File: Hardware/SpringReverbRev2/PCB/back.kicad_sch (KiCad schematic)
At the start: 54 parts, among them IC102 TL074, IC103 TL074, J901 AudioJack2_SwitchT, J902 AudioJack2, J903 AudioJack2, J904 AudioJack2, J905 AudioJack2_SwitchT, J906 AudioJack2, U7 NE5532, U901 L78L05_TO92, X101 RCA, X102 RCA

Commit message: misc corrections
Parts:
- C1, C2: value 10uf -> 10uF; footprint ao_tht:CP_Radial_D6.3mm_P2.50mm -> ao_tht:C_Disc_D3.0mm_W1.6mm_P2.50mm; symbol ao_symbols:CP -> ao_symbols:C
- C101, C109: footprint ao_tht:CP_Radial_D6.3mm_P2.50mm -> ao_tht:C_Disc_D3.0mm_W1.6mm_P2.50mm; symbol ao_symbols:CP -> ao_symbols:C
- C104, C105, C106, C107, C901, C902: value 100n -> 100nF
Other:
- note added: "R109 and R107 set recovery level R107 should be smaller than output coil impedance [sic] 2250/2575Ω: R107 = 22Ω R109 = 22K Increase R109 for stronger output, reduce R109 if circuit distorts even when spring drive is set low."
- note added: "Values for VR1: 800Ω tank: VR1 = 2k 150Ω tank: VR1 = 470Ω Or use 10k trimmer For larger input impedances, try a larger trimmer."
- note removed: "R109 and R107 set recovery level R107 should be smaller than output coil impedance 2250/2575Ω: R107 = 22Ω R109 = 22K Increase R109 for stronger output, reduce R109 if circuit distorts even when spring drive is set low."
- note removed: "Values for R103: 800Ω tank: R103 = 2k 150Ω tank: R103 = 470Ω Or use 10k trimmer For larger input impedances, try a larger trimmer."
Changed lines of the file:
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@@
     (effects (font (size 1.778 1.5113)) (justify left bottom))
   )
-  (text "R109 and R107 set recovery level\nR107 should be smaller than\noutput coil impedance\n2250/2575Ω: R107 = 22Ω R109 = 22K\nIncrease R109 for stronger output,\nreduce R109 if circuit distorts even when\nspring drive is set low."
+  (text "R109 and R107 set recovery level\nR107 should be smaller than\noutput coil impedance [sic]\n2250/2575Ω: R107 = 22Ω R109 = 22K\nIncrease R109 for stronger output,\nreduce R109 if circuit distorts even when\nspring drive is set low."
     (at 89.535 173.355 0)
     (effects (font (size 1.778 1.5113)) (justify left bottom))
@@
     (effects (font (size 1.778 1.5113)) (justify left bottom))
   )
-  (text "Values for R103:\n800Ω tank: R103 = 2k\n150Ω tank: R103 = 470Ω\nOr use 10k trimmer\nFor larger input impedances,\ntry a larger trimmer."
+  (text "Values for VR1:\n800Ω tank: VR1 = 2k\n150Ω tank: VR1 = 470Ω\nOr use 10k trimmer\nFor larger input impedances,\ntry a larger trimmer."
     (at 48.26 153.67 0)
     (effects (font (size 1.778 1.5113)) (justify left top))
@@
       (effects (font (size 1.27 1.27)) (justify left))
     )
-    (property "Value" "100n" (id 1) (at 215.646 102.0322 0)
+    (property "Value" "100nF" (id 1) (at 215.646 102.0322 0)
       (effects (font (size 1.27 1.27)) (justify left))
     )
@@
     )
     (property "Vendor" "Tayda" (id 4) (at 212.725 100.33 0)
+      (effects (font (size 1.27 1.27)) hide)
+    )
+    (property "Description" "Ceramic capacitor" (id 5) (at 212.725 100.33 0)
       (effects (font (size 1.27 1.27)) hide)
     )
@@
       (effects (font (size 1.27 1.27)) hide)
     )
+    (property "Description" "Polyester film capacitor" (id 5) (at 222.25 41.91 0)
+      (effects (font (size 1.27 1.27)) hide)
+    )
     (pin "1")
     (pin "2")
@@
     (pin "2")
   )
-  (symbol (lib_id "ao_symbols:CP") (at 210.82 157.48 270) (unit 1)
+  (symbol (lib_id "ao_symbols:C") (at 210.82 157.48 270) (unit 1)
     (in_bom yes) (on_board yes)
     (property "Reference" "C2" (id 0) (at 212.09 162.56 90)
       (effects (font (size 1.778 1.5113)) (justify left bottom))
     )
-    (property "Value" "10uf" (id 1) (at 210.82 166.37 90)
+    (property "Value" "10uF" (id 1) (at 210.82 166.37 90)
       (effects (font (size 1.778 1.5113)) (justify left bottom))
     )
-    (property "Footprint" "ao_tht:CP_Radial_D6.3mm_P2.50mm" (id 2) (at 207.01 158.4452 0)
+    (property "Footprint" "ao_tht:C_Disc_D3.0mm_W1.6mm_P2.50mm" (id 2) (at 207.01 158.4452 0)
       (effects (font (size 1.27 1.27)) hide)
     )
@@
     )
     (property "Vendor" "Tayda" (id 4) (at 210.82 157.48 0)
+      (effects (font (size 1.27 1.27)) hide)
+    )
+    (property "Description" "Unpolarized electrolytic capacitor" (id 5) (at 210.82 157.48 0)
       (effects (font (size 1.27 1.27)) hide)
     )
@@
     (pin "1")
   )
-  (symbol (lib_id "ao_symbols:CP") (at 210.82 137.16 270) (unit 1)
+  (symbol (lib_id "ao_symbols:C") (at 210.82 137.16 270) (unit 1)
     (in_bom yes) (on_board yes)
     (property "Reference" "C1" (id 0) (at 212.09 142.24 90)
       (effects (font (size 1.778 1.5113)) (justify left bottom))
     )
-    (property "Value" "10uf" (id 1) (at 210.82 146.05 90)
+    (property "Value" "10uF" (id 1) (at 210.82 146.05 90)
       (effects (font (size 1.778 1.5113)) (justify left bottom))
     )
-    (property "Footprint" "ao_tht:CP_Radial_D6.3mm_P2.50mm" (id 2) (at 207.01 138.1252 0)
+    (property "Footprint" "ao_tht:C_Disc_D3.0mm_W1.6mm_P2.50mm" (id 2) (at 207.01 138.1252 0)
       (effects (font (size 1.27 1.27)) hide)
     )
@@
     )
     (property "Vendor" "Tayda" (id 4) (at 210.82 137.16 0)
+      (effects (font (size 1.27 1.27)) hide)
+    )
+    (property "Description" "Unpolarized electrolytic capacitor" (id 5) (at 210.82 137.16 0)
       (effects (font (size 1.27 1.27)) hide)
     )
@@
     )
     (property "Vendor" "Tayda" (id 4) (at 156.21 149.86 0)
+      (effects (font (size 1.27 1.27)) hide)
+    )
+    (property "Description" "Polyester film capacitor" (id 5) (at 156.21 149.86 0)
       (effects (font (size 1.27 1.27)) hide)
     )
@@
       (effects (font (size 1.27 1.27)) hide)
     )
+    (property "Description" "Ceramic capacitor" (id 5) (at 233.68 64.77 0)
+      (effects (font (size 1.27 1.27)) hide)
+    )
     (pin "1")
     (pin "2")
@@
     )
     (property "Vendor" "Tayda" (id 4) (at 207.01 54.61 0)
+      (effects (font (size 1.27 1.27)) hide)
+    )
+    (property "Description" "Polyester film capacitor" (id 5) (at 207.01 54.61 0)
       (effects (font (size 1.27 1.27)) hide)
     )
@@
       (effects (font (size 1.27 1.27)) (justify left))
     )
-    (property "Value" "100n" (id 1) (at 244.221 102.0322 0)
+    (property "Value" "100nF" (id 1) (at 244.221 102.0322 0)
       (effects (font (size 1.27 1.27)) (justify left))
     )
@@
     )
     (property "Vendor" "Tayda" (id 4) (at 241.3 100.33 0)
+      (effects (font (size 1.27 1.27)) hide)
+    )
+    (property "Description" "Ceramic capacitor" (id 5) (at 241.3 100.33 0)
       (effects (font (size 1.27 1.27)) hide)
     )
@@
       (effects (font (size 1.27 1.27)) hide)
     )
+    (property "Description" "Polyester film capacitor" (id 5) (at 73.66 130.81 0)
+      (effects (font (size 1.27 1.27)) hide)
+    )
     (pin "1")
     (pin "2")
@@
       (effects (font (size 1.27 1.27)) (justify left))
     )
-    (property "Value" "100n" (id 1) (at 244.221 94.4122 0)
+    (property "Value" "100nF" (id 1) (at 244.221 94.4122 0)
       (effects (font (size 1.27 1.27)) (justify left))
     )
@@
     )
     (property "Vendor" "Tayda" (id 4) (at 241.3 92.71 0)
+      (effects (font (size 1.27 1.27)) hide)
+    )
+    (property "Description" "Ceramic capacitor" (id 5) (at 241.3 92.71 0)
       (effects (font (size 1.27 1.27)) hide)
     )
@@
       (effects (font (size 1.27 1.27)) (justify left))
     )
-    (property "Value" "100n" (id 1) (at 186.436 94.4122 0)
+    (property "Value" "100nF" (id 1) (at 186.436 94.4122 0)
       (effects (font (size 1.27 1.27)) (justify left))
     )
@@
     )
     (property "Vendor" "Tayda" (id 4) (at 183.515 92.71 0)
+      (effects (font (size 1.27 1.27)) hide)
+    )
+    (property "Description" "Ceramic capacitor" (id 5) (at 183.515 92.71 0)
       (effects (font (size 1.27 1.27)) hide)
     )
@@
     (pin "T")
   )
-  (symbol (lib_id "ao_symbols:CP") (at 38.1 157.48 0) (unit 1)
+  (symbol (lib_id "ao_symbols:C") (at 38.1 157.48 0) (unit 1)
     (in_bom yes) (on_board yes) (fields_autoplaced)
     (property "Reference" "C101" (id 0) (at 41.021 155.7563 0)
@@
       (effects (font (size 1.27 1.27)) (justify left))
     )
-    (property "Footprint" "ao_tht:CP_Radial_D6.3mm_P2.50mm" (id 2) (at 39.0652 161.29 0)
+    (property "Footprint" "ao_tht:C_Disc_D3.0mm_W1.6mm_P2.50mm" (id 2) (at 39.0652 161.29 0)
       (effects (font (size 1.27 1.27)) hide)
     )
@@
     )
     (property "Vendor" "Tayda" (id 4) (at 38.1 157.48 0)
+      (effects (font (size 1.27 1.27)) hide)
+    )
+    (property "Description" "Unpolarized electrolytic capacitor" (id 5) (at 38.1 157.48 0)
       (effects (font (size 1.27 1.27)) hide)
     )
@@
       (effects (font (size 1.27 1.27)) (justify left))
     )
-    (property "Value" "100n" (id 1) (at 186.436 102.0322 0)
+    (property "Value" "100nF" (id 1) (at 186.436 102.0322 0)
       (effects (font (size 1.27 1.27)) (justify left))
     )
@@
     )
     (property "Vendor" "Tayda" (id 4) (at 183.515 100.33 0)
+      (effects (font (size 1.27 1.27)) hide)
+    )
+    (property "Description" "Ceramic capacitor" (id 5) (at 183.515 100.33 0)
       (effects (font (size 1.27 1.27)) hide)
     )
@@
     (pin "3")
   )
-  (symbol (lib_id "ao_symbols:CP") (at 144.78 154.94 0) (mirror x) (unit 1)
+  (symbol (lib_id "ao_symbols:C") (at 144.78 154.94 0) (mirror x) (unit 1)
     (in_bom yes) (on_board yes) (fields_autoplaced)
     (property "Reference" "C109" (id 0) (at 141.859 154.9943 0)
@@
       (effects (font (size 1.27 1.27)) (justify right))
     )
-    (property "Footprint" "ao_tht:CP_Radial_D6.3mm_P2.50mm" (id 2) (at 145.7452 151.13 0)
+    (property "Footprint" "ao_tht:C_Disc_D3.0mm_W1.6mm_P2.50mm" (id 2) (at 145.7452 151.13 0)
       (effects (font (size 1.27 1.27)) hide)
     )
@@
     )
     (property "Vendor" "Tayda" (id 4) (at 144.78 154.94 0)
+      (effects (font (size 1.27 1.27)) hide)
+    )
+    (property "Description" "Unpolarized electrolytic capacitor" (id 5) (at 144.78 154.94 0)
       (effects (font (size 1.27 1.27)) hide)
     )
@@
       (effects (font (size 1.27 1.27)) (justify left))
     )
-    (property "Value" "100n" (id 1) (at 215.646 94.4122 0)
+    (property "Value" "100nF" (id 1) (at 215.646 94.4122 0)
       (effects (font (size 1.27 1.27)) (justify left))
     )
@@
       (effects (font (size 1.27 1.27)) hide)
     )
+    (property "Description" "Ceramic capacitor" (id 5) (at 212.725 92.71 0)
+      (effects (font (size 1.27 1.27)) hide)
+    )

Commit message: Backlog
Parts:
- removed JP101: Conn_01x04, Connector_Molex:Molex_KK-254_AE-6410-04A_1x04_P2.54mm_Vertical, symbol Connector_Generic:Conn_01x04
- removed JP102: Conn_01x03, ao_tht:Molex_KK-254_AE-6410-03A_1x03_P2.54mm_Vertical, symbol Connector_Generic:Conn_01x03
- removed LED1: LED_green, ao_tht:LED_D5.0mm, symbol ao_symbols:LED_green
- C1, C101, C104, C105, C106, C107, C109, C2, C901, C902: footprint ao_tht:C_Disc_D3.0mm_W1.6mm_P2.50mm -> AO_tht:C_Disc_D3.0mm_W1.6mm_P2.50mm; symbol ao_symbols:C -> AO_symbols:C
- C108, C110, C3, C4: footprint ao_tht:C_Rect_L7.2mm_W2.5mm_P5.00mm_FKS2_FKP2_MKS2_MKP2 -> AO_tht:C_Disc_D3.0mm_W1.6mm_P2.50mm; symbol ao_symbols:C -> AO_symbols:C
- C5: footprint ao_tht:C_Disc_D5.0mm_W2.5mm_P5.00mm -> AO_tht:C_Disc_D3.0mm_W1.6mm_P2.50mm; symbol ao_symbols:C -> AO_symbols:C
- GRAF901: symbol ao_symbols:Graphic -> AO_symbols:Graphic
- H901, H902: footprint ao_tht:MountingHole_3.2mm_M3 -> AO_tht:MountingHole_3.2mm_M3; symbol ao_symbols:MountingHole -> AO_symbols:MountingHole
- IC102, IC103: footprint ao_tht:DIP-14_W7.62mm_Socket_LongPads -> AO_tht:DIP-14_W7.62mm_Socket_LongPads; symbol ao_symbols:TL074 -> AO_symbols:TL074
- J901, J905: footprint ao_tht:Jack_6.35mm_PJ_629HAN_slots -> AO_tht:Jack_6.35mm_PJ_629HAN_slots; symbol ao_symbols:AudioJack2_SwitchT -> AO_symbols:AudioJack2_SwitchT
- J902, J903, J904, J906: footprint ao_tht:Jack_6.35mm_PJ_629HAN_slots -> AO_tht:Jack_6.35mm_PJ_629HAN_slots; symbol ao_symbols:AudioJack2 -> AO_symbols:AudioJack2
- R10, R101, R102, R103, R104, R105, R106, R107, R108, R109, R11, R110, R18, R19, R3, R6, R901, R902: footprint ao_tht:R_Axial_DIN0207_L6.3mm_D2.5mm_P10.16mm_Horizontal -> AO_tht:R_Axial_DIN0207_L6.3mm_D2.5mm_P10.16mm_Horizontal; symbol ao_symbols:R -> AO_symbols:R
- U7: footprint ao_tht:DIP-8_W7.62mm_Socket_LongPads -> AO_tht:DIP-8_W7.62mm_Socket_LongPads
- U901: footprint ao_tht:TO-92_Inline_Wide -> AO_tht:TO-92_Inline_Wide; symbol ao_symbols:L78L05_TO92 -> AO_symbols:L78L05_TO92
- V101: footprint ao_tht:Vactrol_VTL5C -> AO_tht:Vactrol_VTL5C; symbol ao_symbols:Vactrol -> AO_symbols:Vactrol
- X101: symbol ao_symbols:AudioJack2 -> AO_symbols:AudioJack2; Manufacturer (none) -> CUI; Part (none) -> RCJ-023; SKU A-1121 -> CP-1408-ND; Vendor Tayda -> Digi-Key
- X102: symbol ao_symbols:AudioJack2 -> AO_symbols:AudioJack2; Manufacturer (none) -> CUI; Part (none) -> RCJ-022; SKU A-1121 -> CP-1407-ND; Vendor Tayda -> Digi-Key
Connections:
- net VAC_AN_B: now also V101.2 (+)
- net MIXPOT_WET_B: now reaches C110.2, IC102.7, R109.2
- net MIXPOT_DRY_B: now reaches IC103.8, R108.2
- net TO_TANK_S_B: now reaches C108.1, IC102.8, X101.S
- net +5V: now reaches U901.1 (VO), Z$102.1 (+5VDC)
- net FROM_TANK renamed FROM_TANK_T_B
- net REVERB_RETURN renamed MIXPOT_MIX_B
- net TO_TANK renamed TO_TANK_T_B
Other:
- moved on the sheet: C104, C105, C106, C107, C901, C902, IC102E, IC103A, IC103B, IC103E, R10, R11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

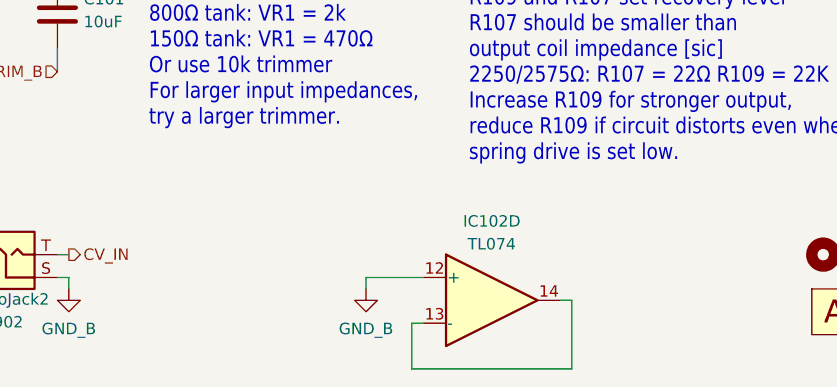
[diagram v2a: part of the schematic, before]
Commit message: Bigger tone knob; hardware
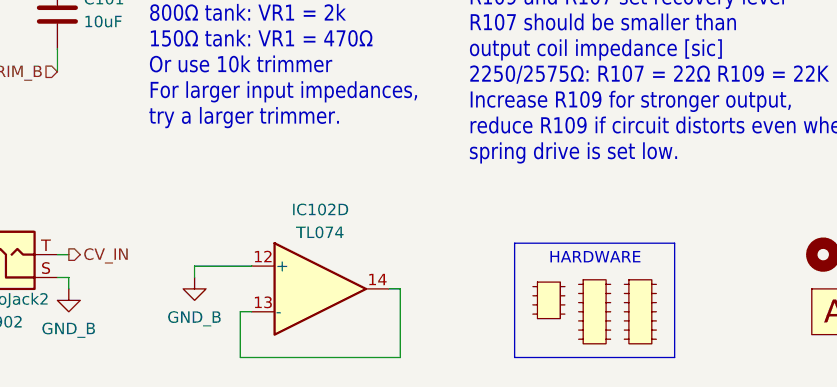
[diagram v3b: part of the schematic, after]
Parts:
- added J917: DIP-8, symbol AO_symbols:DIP-8
- added J919, J920: DIP-14, symbol AO_symbols:DIP-14
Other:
- note added: "HARDWARE"
- moved on the sheet: IC102D
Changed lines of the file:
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@@
     (stroke (width 0) (type default))
   )
-  (wire (pts (xy 78.74 191.77) (xy 77.47 191.77))
+  (wire (pts (xy 59.69 190.5) (xy 58.42 190.5))
     (stroke (width 0) (type default))
   )
@@
     (stroke (width 0) (type default))
   )
-  (wire (pts (xy 72.39 187.96) (xy 72.39 186.69))
+  (wire (pts (xy 53.34 186.69) (xy 53.34 185.42))
     (stroke (width 0) (type default))
   )
@@
     (stroke (width 0) (type default))
   )
-  (wire (pts (xy 77.47 196.85) (xy 95.25 196.85))
+  (wire (pts (xy 58.42 195.58) (xy 76.2 195.58))
     (stroke (width 0) (type default))
   )
@@
     (stroke (width 0) (type default))
   )
-  (wire (pts (xy 95.25 189.23) (xy 93.98 189.23))
+  (wire (pts (xy 76.2 187.96) (xy 74.93 187.96))
     (stroke (width 0) (type default))
   )
@@
     (stroke (width 0) (type default))
   )
-  (wire (pts (xy 72.39 186.69) (xy 78.74 186.69))
+  (wire (pts (xy 53.34 185.42) (xy 59.69 185.42))
     (stroke (width 0) (type default))
   )
@@
     (stroke (width 0) (type default))
   )
-  (wire (pts (xy 95.25 196.85) (xy 95.25 189.23))
+  (wire (pts (xy 76.2 195.58) (xy 76.2 187.96))
     (stroke (width 0) (type default))
   )
@@
     (stroke (width 0) (type default))
   )
-  (wire (pts (xy 77.47 191.77) (xy 77.47 196.85))
+  (wire (pts (xy 58.42 190.5) (xy 58.42 195.58))
     (stroke (width 0) (type default))
   )
@@
     (stroke (width 0) (type default))
   )
+  (rectangle (start 88.9 182.88) (end 106.68 195.58)
+    (stroke (width 0) (type default))
+    (fill (type none))
+  )
   (text "Reverb Board" (at 177.8 26.67 0)
     (effects (font (size 2.54 2.159)) (justify left bottom))
   )
+  (text "HARDWARE" (at 92.71 185.42 0)
+    (effects (font (size 1.27 1.27)) (justify left bottom))
+  )
   (text "Close solder jumper if\nBrick is not installed\nto stabilise unused\nop amp gate"
     (at 88.9 118.11 0)
@@
     )
   )
-  (symbol (lib_id "AO_symbols:TL074") (at 86.36 189.23 0) (unit 4)
+  (symbol (lib_id "AO_symbols:TL074") (at 67.31 187.96 0) (unit 4)
     (in_bom yes) (on_board yes) (dnp no) (fields_autoplaced)
-    (property "Reference" "IC102" (at 86.36 180.4502 0)
+    (property "Reference" "IC102" (at 67.31 179.1802 0)
       (effects (font (size 1.27 1.27)))
     )
-    (property "Value" "TL074" (at 86.36 182.9871 0)
+    (property "Value" "TL074" (at 67.31 181.7171 0)
       (effects (font (size 1.27 1.27)))
     )
-    (property "Footprint" "AO_tht:DIP-14_W7.62mm_Socket_LongPads" (at 85.09 186.69 0)
+    (property "Footprint" "AO_tht:DIP-14_W7.62mm_Socket_LongPads" (at 66.04 185.42 0)
       (effects (font (size 1.27 1.27)) hide)
     )
-    (property "Datasheet" "" (at 87.63 184.15 0)
+    (property "Datasheet" "" (at 68.58 182.88 0)
       (effects (font (size 1.27 1.27)) hide)
     )
-    (property "Vendor" "Tayda" (at 86.36 189.23 0)
+    (property "Vendor" "Tayda" (at 67.31 187.96 0)
       (effects (font (size 1.27 1.27)) hide)
     )
-    (property "SKU" "A-1138" (at 86.36 189.23 0)
+    (property "SKU" "A-1138" (at 67.31 187.96 0)
       (effects (font (size 1.27 1.27)) hide)
     )
-    (property "Manufacturer" "" (at 86.36 189.23 0)
+    (property "Manufacturer" "" (at 67.31 187.96 0)
       (effects (font (size 1.27 1.27)) hide)
     )
-    (property "Part" "" (at 86.36 189.23 0)
+    (property "Part" "" (at 67.31 187.96 0)
       (effects (font (size 1.27 1.27)) hide)
     )
@@
     )
   )
+  (symbol (lib_id "AO_symbols:DIP-14") (at 97.79 190.5 0) (unit 1)
+    (in_bom yes) (on_board yes) (dnp no) (fields_autoplaced)
+    (property "Reference" "J919" (at 97.79 189.484 0)
+      (effects (font (size 1.27 1.27)) hide)
+    )
+    (property "Value" "DIP-14" (at 97.79 191.77 0)
+      (effects (font (size 1.27 1.27)) hide)
+    )
+    (property "Footprint" "" (at 97.79 192.024 0)
+      (effects (font (size 1.27 1.27)) hide)
+    )
+    (property "Datasheet" "" (at 97.79 192.024 0)
+      (effects (font (size 1.27 1.27)) hide)
+    )
+    (instances
+      (project "springReverbRev2"
+        (path "/7cc2117a-75f3-473b-aa3c-f6f0c8514e37/757cdb0d-1f9d-4951-b906-b680c7b834f3"
+          (reference "J919") (unit 1)
+        )
+        (path "/7cc2117a-75f3-473b-aa3c-f6f0c8514e37/cb7e7ca4-1a75-4992-9aba-d7df48630a9d"
+          (reference "J919") (unit 1)
+        )
+      )
+    )
+  )
   (symbol (lib_id "aaaSpringReverb:GND_B") (at 144.78 168.91 0) (unit 1)
     (in_bom yes) (on_board yes) (dnp no) (fields_autoplaced)
@@
     )
   )
+  (symbol (lib_id "AO_symbols:DIP-8") (at 92.71 189.23 0) (unit 1)
+    (in_bom yes) (on_board yes) (dnp no) (fields_autoplaced)
+    (property "Reference" "J917" (at 92.71 187.96 0)
+      (effects (font (size 1.27 1.27)) hide)
+    )
+    (property "Value" "DIP-8" (at 92.71 190.246 0)
+      (effects (font (size 1.27 1.27)) hide)
+    )
+    (property "Footprint" "" (at 92.71 189.23 0)
+      (effects (font (size 1.27 1.27)) hide)
+    )
+    (property "Datasheet" "" (at 92.71 189.23 0)
+      (effects (font (size 1.27 1.27)) hide)
+    )
+    (instances
+      (project "springReverbRev2"
+        (path "/7cc2117a-75f3-473b-aa3c-f6f0c8514e37/757cdb0d-1f9d-4951-b906-b680c7b834f3"
+          (reference "J917") (unit 1)
+        )
+        (path "/7cc2117a-75f3-473b-aa3c-f6f0c8514e37/cb7e7ca4-1a75-4992-9aba-d7df48630a9d"
+          (reference "J917") (unit 1)
+        )
+      )
+    )
+  )
   (symbol (lib_id "SpringReverbRev2_combined-eagle-import:UP_PHASE_SPIKE") (at 86.36 130.81 0) (unit 1)
     (in_bom yes) (on_board yes) (dnp no)
@@
     )
   )
+  (symbol (lib_id "AO_symbols:DIP-14") (at 102.87 190.5 0) (unit 1)
+    (in_bom yes) (on_board yes) (dnp no) (fields_autoplaced)
+    (property "Reference" "J920" (at 102.87 189.484 0)
+      (effects (font (size 1.27 1.27)) hide)
+    )
+    (property "Value" "DIP-14" (at 102.87 191.77 0)
+      (effects (font (size 1.27 1.27)) hide)
+    )
+    (property "Footprint" "" (at 102.87 192.024 0)
+      (effects (font (size 1.27 1.27)) hide)
+    )
+    (property "Datasheet" "" (at 102.87 192.024 0)
+      (effects (font (size 1.27 1.27)) hide)
+    )
+    (instances
+      (project "springReverbRev2"
+        (path "/7cc2117a-75f3-473b-aa3c-f6f0c8514e37/757cdb0d-1f9d-4951-b906-b680c7b834f3"
+          (reference "J920") (unit 1)
+        )
+        (path "/7cc2117a-75f3-473b-aa3c-f6f0c8514e37/cb7e7ca4-1a75-4992-9aba-d7df48630a9d"
+          (reference "J918") (unit 1)
+        )
+      )
+    )
+  )
   (symbol (lib_id "SpringReverbRev2_combined-eagle-import:UP_PHASE_SPIKE") (at 139.7 125.73 0) (unit 1)
     (in_bom yes) (on_board yes) (dnp no)
@@
     )
   )
-  (symbol (lib_id "aaaSpringReverb:GND_B") (at 72.39 187.96 0) (unit 1)
+  (symbol (lib_id "aaaSpringReverb:GND_B") (at 53.34 186.69 0) (unit 1)
     (in_bom yes) (on_board yes) (dnp no) (fields_autoplaced)
-    (property "Reference" "#PWR0110" (at 72.39 194.31 0)
+    (property "Reference" "#PWR0110" (at 53.34 193.04 0)
       (effects (font (size 1.27 1.27)) hide)
     )
-    (property "Value" "GND_B" (at 72.39 192.4034 0)
+    (property "Value" "GND_B" (at 53.34 191.1334 0)
       (effects (font (size 1.27 1.27)))
     )
-    (property "Footprint" "" (at 72.39 187.96 0)
+    (property "Footprint" "" (at 53.34 186.69 0)
       (effects (font (size 1.27 1.27)) hide)
     )
-    (property "Datasheet" "" (at 72.39 187.96 0)
+    (property "Datasheet" "" (at 53.34 186.69 0)
       (effects (font (size 1.27 1.27)) hide)
     )
